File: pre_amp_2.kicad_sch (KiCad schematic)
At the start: 55 parts, among them J1 IN, J10 SW2_3, J11 SW2_1, J12 SW2_4, J13 VR5_3, J14 VR5_1, J15 OUT, J2 GND2, J3 Vin, J4 GND, J5 VR3_2, J6 VR3_3, J7 VR1_3, J9 VR4_2, SW1 bright, SW2 SW_SP3T, U1 TL072, U3 TC1044S

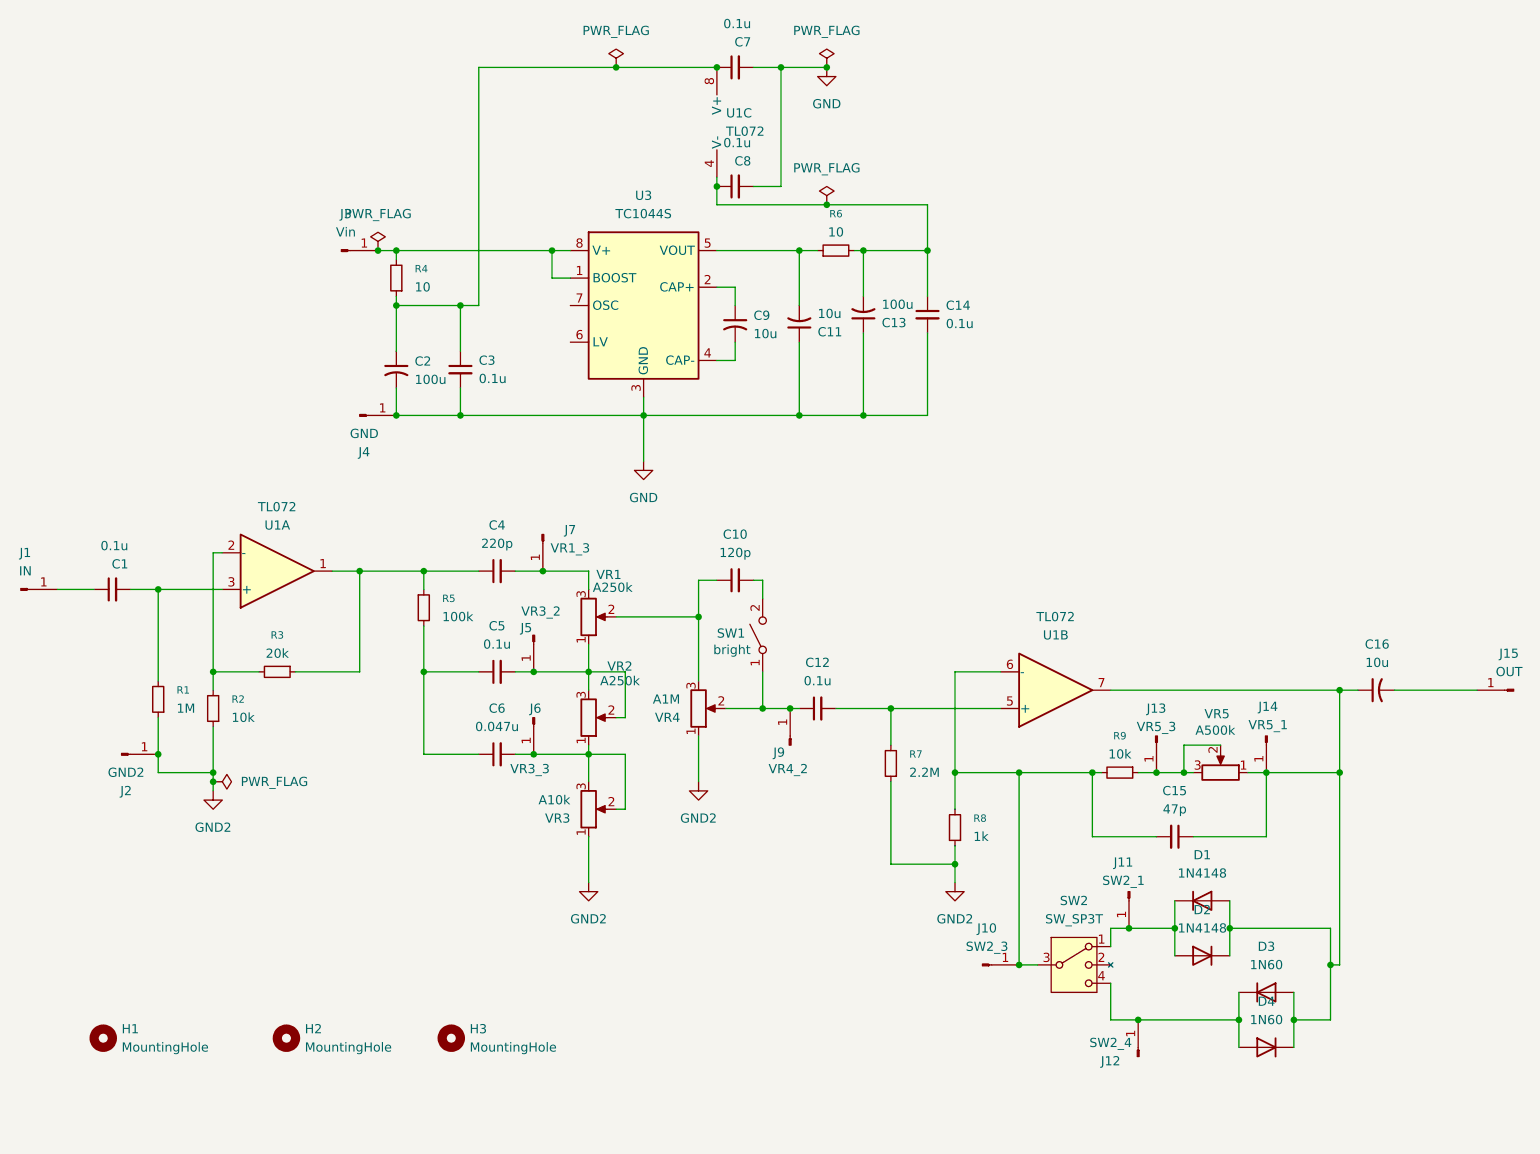
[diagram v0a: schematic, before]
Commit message: 67番ピンに330pを追加、ICパッケージのすぐ横に付ける
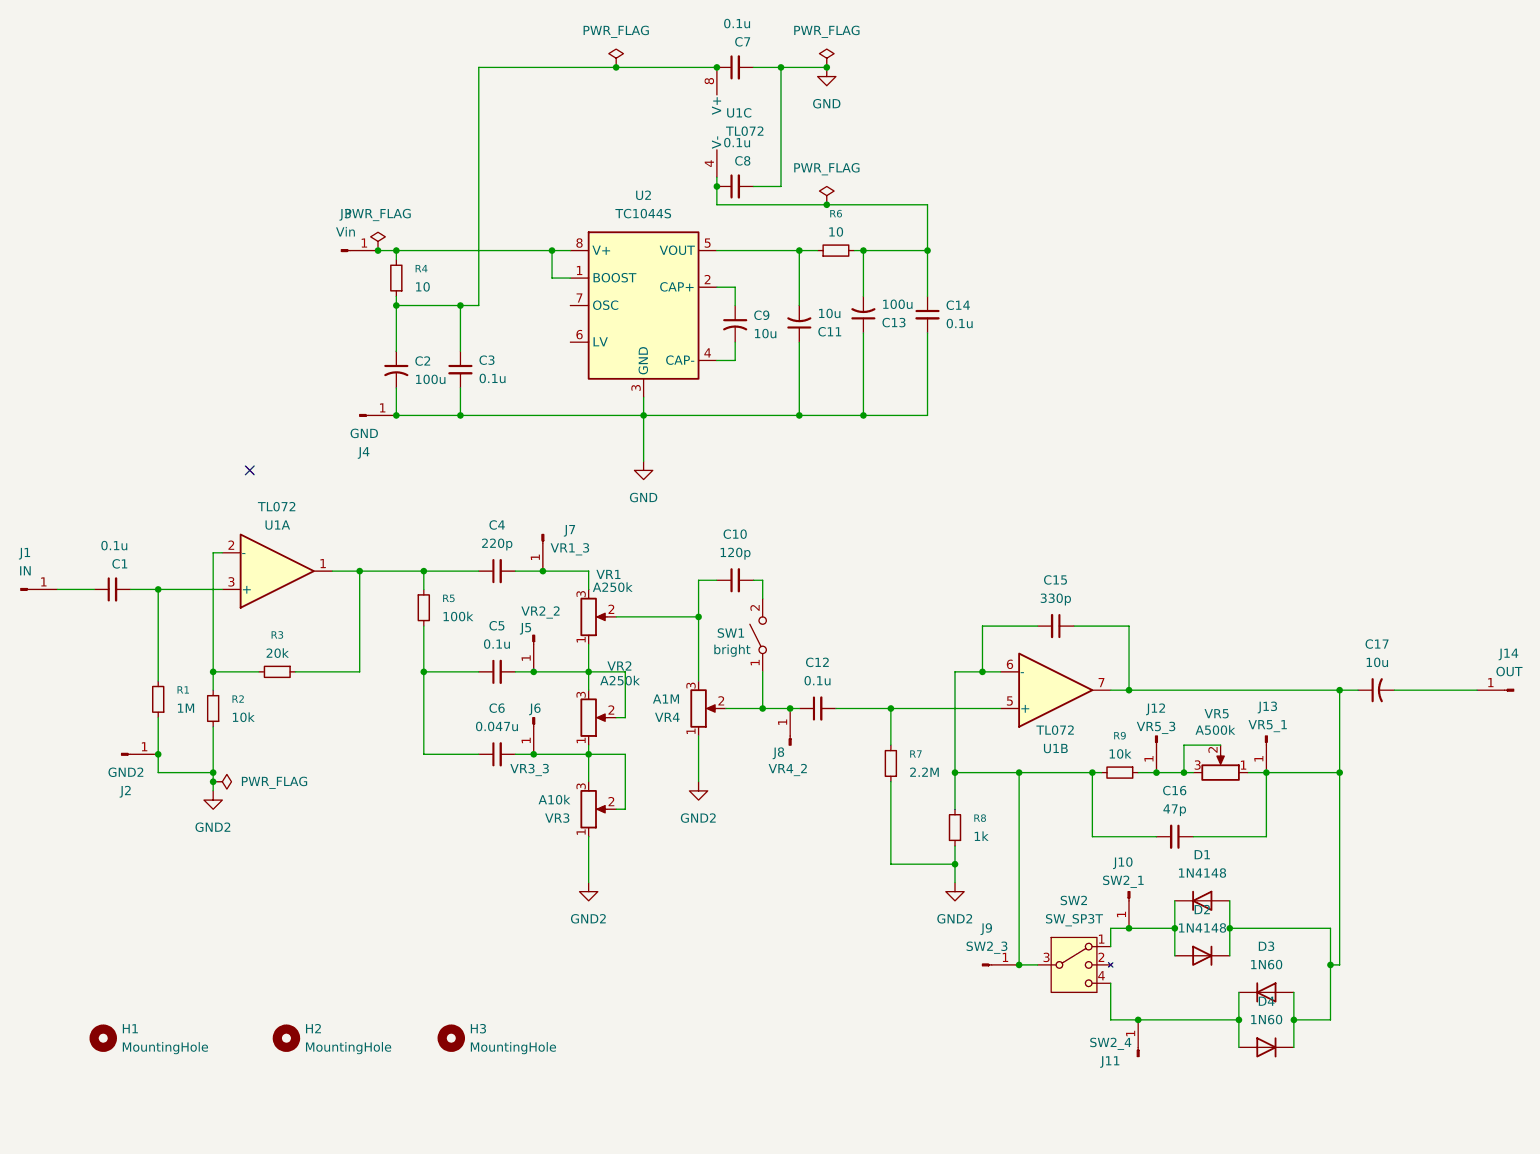
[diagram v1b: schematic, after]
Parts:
- added C15: 330p, symbol Device:C_Small
- J5: value VR3_2 -> VR2_2
- renumbered C15 to C16, C16 to C17, J11 to J10, J12 to J11, J13 to J12, J14 to J13, J15 to J14, J9 to J8, J10 to J9, U3 to U2
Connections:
- net at C16.1, C17.1, D1.2 (A)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: now also C15.1
- net at C16.2, J9.1 (Pin_1), R8.2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: now also C15.2
- no-connect marks 0 -> 1
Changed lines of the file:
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@@
 	)
 	(junction
+		(at 162.56 102.87)
+		(diameter 0)
+		(color 0 0 0 0)
+	)
+	(junction
 		(at 196.85 138.43)
 		(diameter 0)
@@
 	)
 	(junction
+		(at 182.88 105.41)
+		(diameter 0)
+		(color 0 0 0 0)
+	)
+	(junction
 		(at 140.97 19.05)
 		(diameter 0)
@@
 		(color 0 0 0 0)
 	)
+	(no_connect
+		(at 60.96 74.93)
+	)
 	(wire
 		(pts
@@
 	(wire
 		(pts
+			(xy 182.88 105.41) (xy 212.09 105.41)
+		)
+		(stroke
+			(width 0)
+			(type default)
+		)
+	)
+	(wire
+		(pts
 			(xy 81.28 63.5) (xy 81.28 67.31)
 		)
@@
 	(wire
 		(pts
+			(xy 162.56 96.52) (xy 162.56 102.87)
+		)
+		(stroke
+			(width 0)
+			(type default)
+		)
+	)
+	(wire
+		(pts
 			(xy 177.8 116.84) (xy 179.07 116.84)
 		)
@@
 	(wire
 		(pts
-			(xy 158.75 102.87) (xy 165.1 102.87)
+			(xy 158.75 102.87) (xy 162.56 102.87)
+		)
+		(stroke
+			(width 0)
+			(type default)
+		)
+	)
+	(wire
+		(pts
+			(xy 182.88 96.52) (xy 182.88 105.41)
+		)
+		(stroke
+			(width 0)
+			(type default)
+		)
+	)
+	(wire
+		(pts
+			(xy 162.56 102.87) (xy 165.1 102.87)
 		)
 		(stroke
@@
 	(wire
 		(pts
+			(xy 175.26 96.52) (xy 182.88 96.52)
+		)
+		(stroke
+			(width 0)
+			(type default)
+		)
+	)
+	(wire
+		(pts
 			(xy 125.73 44.45) (xy 137.16 44.45)
 		)
@@
 	(wire
 		(pts
+			(xy 170.18 96.52) (xy 162.56 96.52)
+		)
+		(stroke
+			(width 0)
+			(type default)
+		)
+	)
+	(wire
+		(pts
 			(xy 125.73 35.56) (xy 125.73 34.29)
 		)
@@
 	(wire
 		(pts
-			(xy 180.34 105.41) (xy 212.09 105.41)
+			(xy 180.34 105.41) (xy 182.88 105.41)
 		)
 		(stroke
@@
 	)
 	(symbol
+		(lib_id "Device:C_Small")
+		(at 172.72 96.52 270)
+		(unit 1)
+		(exclude_from_sim no)
+		(in_bom yes)
+		(on_board yes)
+		(dnp no)
+		(fields_autoplaced yes)
+		(property "Reference" "C15"
+			(at 172.7136 90.17 90)
+			(effects
+				(font
+					(size 1.27 1.27)
+				)
+			)
+		)
+		(property "Value" "330p"
+			(at 172.7136 92.71 90)
+			(effects
+				(font
+					(size 1.27 1.27)
+				)
+			)
+		)
+		(property "Footprint" ""
+			(at 172.72 96.52 0)
+			(effects
+				(font
+					(size 1.27 1.27)
+				)
+				(hide yes)
+			)
+		)
+		(property "Datasheet" "~"
+			(at 172.72 96.52 0)
+			(effects
+				(font
+					(size 1.27 1.27)
+				)
+				(hide yes)
+			)
+		)
+		(property "Description" "Unpolarized capacitor, small symbol"
+			(at 172.72 96.52 0)
+			(effects
+				(font
+					(size 1.27 1.27)
+				)
+				(hide yes)
+			)
+		)
+		(pin "1"
+		)
+		(pin "2"
+		)
+		(instances
+			(project "pre_amp_2"
+				(path "/a24a43ce-b78c-4b02-8ea5-638bfbce1c81"
+					(reference "C15")
+					(unit 1)
+				)
+			)
+		)
+	)
+	(symbol
 		(lib_id "power:PWR_FLAG")
 		(at 140.97 38.1 0)
@@
 		(on_board yes)
 		(dnp no)
-		(property "Reference" "J12"
+		(property "Reference" "J11"
 			(at 180.34 156.845 90)
 			(effects
@@
 			(project "pre_amp_2"
 				(path "/a24a43ce-b78c-4b02-8ea5-638bfbce1c81"
-					(reference "J12")
+					(reference "J11")
 					(unit 1)
 				)
@@
 		(on_board yes)
 		(dnp no)
-		(property "Reference" "J10"
+		(property "Reference" "J9"
 			(at 163.195 138.43 0)
 			(effects
@@
 			(project "pre_amp_2"
 				(path "/a24a43ce-b78c-4b02-8ea5-638bfbce1c81"
-					(reference "J10")
+					(reference "J9")
 					(unit 1)
 				)
@@
 		(dnp no)
 		(fields_autoplaced yes)
-		(property "Reference" "U3"
+		(property "Reference" "U2"
 			(at 115.57 36.83 0)
 			(effects
@@
 			(project ""
 				(path "/a24a43ce-b78c-4b02-8ea5-638bfbce1c81"
-					(reference "U3")
+					(reference "U2")
 					(unit 1)
 				)
@@
 		(on_board yes)
 		(dnp no)
-		(property "Reference" "J11"
+		(property "Reference" "J10"
 			(at 182.118 129.286 90)
 			(effects
@@
 			(project "pre_amp_2"
 				(path "/a24a43ce-b78c-4b02-8ea5-638bfbce1c81"
-					(reference "J11")
+					(reference "J10")
 					(unit 1)
 				)
@@
 		(dnp no)
 		(fields_autoplaced yes)
-		(property "Reference" "C16"
+		(property "Reference" "C17"
 			(at 217.297 99.06 90)
 			(effects
@@
 			(project "pre_amp_2"
 				(path "/a24a43ce-b78c-4b02-8ea5-638bfbce1c81"
-					(reference "C16")
+					(reference "C17")
 					(unit 1)
 				)
@@
 		(on_board yes)
 		(dnp no)
-		(property "Reference" "J14"
+		(property "Reference" "J13"
 			(at 202.184 107.696 90)
 			(effects
@@
 			(project "pre_amp_2"
 				(path "/a24a43ce-b78c-4b02-8ea5-638bfbce1c81"
-					(reference "J14")
+					(reference "J13")
 					(unit 1)
 				)
@@
 		(dnp no)
 		(property "Reference" "U1"
-			(at 172.72 97.79 0)
+			(at 172.72 113.538 0)
 			(effects
 				(font
@@
 		)
 		(property "Value" "TL072"
-			(at 172.72 95.25 0)
+			(at 172.72 110.998 0)
 			(effects
 				(font
@@
 		(dnp no)
 		(fields_autoplaced yes)
-		(property "Reference" "C15"
+		(property "Reference" "C16"
 			(at 189.2236 119.38 90)
 			(effects
@@
 			(project "pre_amp_2"
 				(path "/a24a43ce-b78c-4b02-8ea5-638bfbce1c81"
-					(reference "C15")
+					(reference "C16")
 					(unit 1)
 				)
@@
 		(on_board yes)
 		(dnp no)
-		(property "Reference" "J9"
+		(property "Reference" "J8"
 			(at 134.366 114.046 90)
 			(effects
@@
 			(project "pre_amp_2"
 				(path "/a24a43ce-b78c-4b02-8ea5-638bfbce1c81"
-					(reference "J9")
+					(reference "J8")
 					(unit 1)
 				)
@@
 		(dnp no)
 		(fields_autoplaced yes)
-		(property "Reference" "J15"
+		(property "Reference" "J14"
 			(at 235.585 100.33 0)
 			(effects
@@
 			(project "pre_amp_2"
 				(path "/a24a43ce-b78c-4b02-8ea5-638bfbce1c81"
-					(reference "J15")
+					(reference "J14")
 					(unit 1)
 				)
@@
 			)
 		)
-		(property "Value" "VR3_2"
+		(property "Value" "VR2_2"
 			(at 101.346 94.488 90)
 			(effects
@@
 		(on_board yes)
 		(dnp no)
-		(property "Reference" "J13"
+		(property "Reference" "J12"
 			(at 186.69 107.95 90)
 			(effects
@@
 			(project "pre_amp_2"
 				(path "/a24a43ce-b78c-4b02-8ea5-638bfbce1c81"
-					(reference "J13")
+					(reference "J12")
 					(unit 1)
 				)

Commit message: 発振対策で初段の増幅率を上げて後段のボリュームと抵抗の値を調整
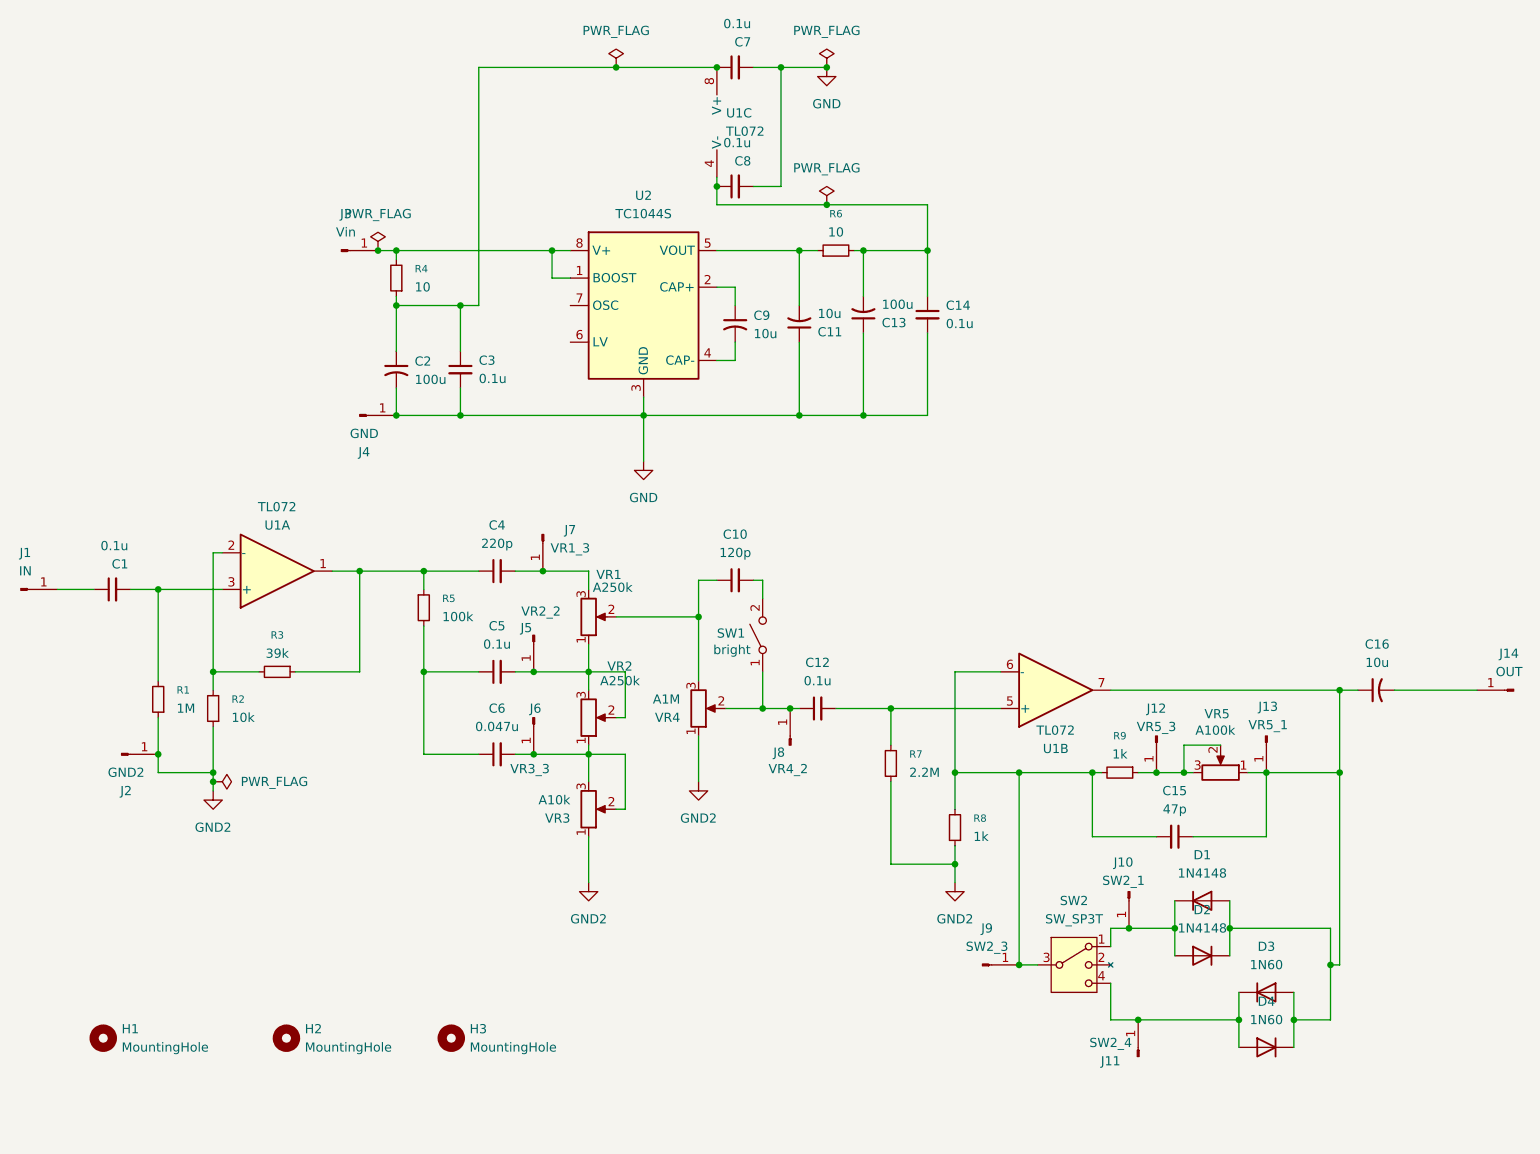
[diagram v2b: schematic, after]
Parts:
- removed C15: 330p, symbol Device:C_Small
- R3: value 20k -> 39k
- R9: value 10k -> 1k
- VR5: value A500k -> A100k
- renumbered C16 to C15, C17 to C16
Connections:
- no-connect marks 1 -> 0
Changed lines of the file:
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@@
 	)
 	(junction
-		(at 162.56 102.87)
-		(diameter 0)
-		(color 0 0 0 0)
-	)
-	(junction
 		(at 196.85 138.43)
 		(diameter 0)
@@
 	)
 	(junction
-		(at 182.88 105.41)
-		(diameter 0)
-		(color 0 0 0 0)
-	)
-	(junction
 		(at 140.97 19.05)
 		(diameter 0)
@@
 		(color 0 0 0 0)
 	)
-	(no_connect
-		(at 60.96 74.93)
-	)
 	(wire
 		(pts
@@
 	(wire
 		(pts
-			(xy 182.88 105.41) (xy 212.09 105.41)
-		)
-		(stroke
-			(width 0)
-			(type default)
-		)
-	)
-	(wire
-		(pts
 			(xy 81.28 63.5) (xy 81.28 67.31)
 		)
@@
 	(wire
 		(pts
-			(xy 162.56 96.52) (xy 162.56 102.87)
-		)
-		(stroke
-			(width 0)
-			(type default)
-		)
-	)
-	(wire
-		(pts
 			(xy 177.8 116.84) (xy 179.07 116.84)
 		)
@@
 	(wire
 		(pts
-			(xy 158.75 102.87) (xy 162.56 102.87)
-		)
-		(stroke
-			(width 0)
-			(type default)
-		)
-	)
-	(wire
-		(pts
-			(xy 182.88 96.52) (xy 182.88 105.41)
-		)
-		(stroke
-			(width 0)
-			(type default)
-		)
-	)
-	(wire
-		(pts
-			(xy 162.56 102.87) (xy 165.1 102.87)
+			(xy 158.75 102.87) (xy 165.1 102.87)
 		)
 		(stroke
@@
 	(wire
 		(pts
-			(xy 175.26 96.52) (xy 182.88 96.52)
-		)
-		(stroke
-			(width 0)
-			(type default)
-		)
-	)
-	(wire
-		(pts
 			(xy 125.73 44.45) (xy 137.16 44.45)
 		)
@@
 	(wire
 		(pts
-			(xy 170.18 96.52) (xy 162.56 96.52)
-		)
-		(stroke
-			(width 0)
-			(type default)
-		)
-	)
-	(wire
-		(pts
 			(xy 125.73 35.56) (xy 125.73 34.29)
 		)
@@
 	(wire
 		(pts
-			(xy 180.34 105.41) (xy 182.88 105.41)
+			(xy 180.34 105.41) (xy 212.09 105.41)
 		)
 		(stroke
@@
 	)
 	(symbol
-		(lib_id "Device:C_Small")
-		(at 172.72 96.52 270)
-		(unit 1)
-		(exclude_from_sim no)
-		(in_bom yes)
-		(on_board yes)
-		(dnp no)
-		(fields_autoplaced yes)
-		(property "Reference" "C15"
-			(at 172.7136 90.17 90)
-			(effects
-				(font
-					(size 1.27 1.27)
-				)
-			)
-		)
-		(property "Value" "330p"
-			(at 172.7136 92.71 90)
-			(effects
-				(font
-					(size 1.27 1.27)
-				)
-			)
-		)
-		(property "Footprint" ""
-			(at 172.72 96.52 0)
-			(effects
-				(font
-					(size 1.27 1.27)
-				)
-				(hide yes)
-			)
-		)
-		(property "Datasheet" "~"
-			(at 172.72 96.52 0)
-			(effects
-				(font
-					(size 1.27 1.27)
-				)
-				(hide yes)
-			)
-		)
-		(property "Description" "Unpolarized capacitor, small symbol"
-			(at 172.72 96.52 0)
-			(effects
-				(font
-					(size 1.27 1.27)
-				)
-				(hide yes)
-			)
-		)
-		(pin "1"
-		)
-		(pin "2"
-		)
-		(instances
-			(project "pre_amp_2"
-				(path "/a24a43ce-b78c-4b02-8ea5-638bfbce1c81"
-					(reference "C15")
-					(unit 1)
-				)
-			)
-		)
-	)
-	(symbol
 		(lib_id "power:PWR_FLAG")
 		(at 140.97 38.1 0)
@@
 			)
 		)
-		(property "Value" "20k"
+		(property "Value" "39k"
 			(at 64.77 100.33 90)
 			(effects
@@
 		(dnp no)
 		(fields_autoplaced yes)
-		(property "Reference" "C17"
+		(property "Reference" "C16"
 			(at 217.297 99.06 90)
 			(effects
@@
 			(project "pre_amp_2"
 				(path "/a24a43ce-b78c-4b02-8ea5-638bfbce1c81"
-					(reference "C17")
+					(reference "C16")
 					(unit 1)
 				)
@@
 		(dnp no)
 		(fields_autoplaced yes)
-		(property "Reference" "C16"
+		(property "Reference" "C15"
 			(at 189.2236 119.38 90)
 			(effects
@@
 			(project "pre_amp_2"
 				(path "/a24a43ce-b78c-4b02-8ea5-638bfbce1c81"
-					(reference "C16")
+					(reference "C15")
 					(unit 1)
 				)
@@
 			)
 		)
-		(property "Value" "10k"
+		(property "Value" "1k"
 			(at 181.61 114.3 90)
 			(effects
@@
 			)
 		)
-		(property "Value" "A500k"
+		(property "Value" "A100k"
 			(at 197.612 110.998 90)
 			(effects
